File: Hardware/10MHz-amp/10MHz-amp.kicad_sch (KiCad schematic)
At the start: 118 parts, among them J1 Conn_Coaxial, J2 Barrel_Jack_MountingPin, J3 BANANA_JACK, J4 BANANA_JACK, J5 BANANA_JACK, J6 Conn_Coaxial, J7 Conn_01x07_Pin, J8 Conn_01x07_Socket, K1 TQ2-24V, K2 TQ2-24V, K3 TQ2-24V, K4 TQ2-24V, K5 TQ2-24V, K6 TQ2-5V, Q1 PMOS, Q2 PMOS, Q3 NMOS, SW1 SW_SPDT, SW2 SW_SPST, SW3 SW_SP5T_NR01105, U1 THS3491xDDA

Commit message: fixed issues 1-5 and changed relay topo
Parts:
- removed C15: 6.8u, Capacitor_SMD:C_0603_1608Metric, symbol Device:C
- removed D3, D4: PTVS18VZ1USK, Diode_SMD:Nexperia_DSN1608-2_1.6x0.8mm, symbol Diode:PTVS18VZ1USK
- removed D5: PTVS15VZ1USK, Diode_SMD:Nexperia_DSN1608-2_1.6x0.8mm, symbol Diode:PTVS15VZ1USK
- removed D6, D8, D9: D_Zener, Diode_SMD:D_0603_1608Metric, symbol Device:D_Zener
- removed F1: Fuse, symbol Device:Fuse
- removed Q1: PMOS, symbol Simulation_SPICE:PMOS
- removed R8: 10k, Capacitor_SMD:C_0603_1608Metric, symbol Device:R
- added C12: 6.8u, Capacitor_SMD:C_0603_1608Metric, symbol Device:C
- added D13, D26: SMAJ16CA, Diode_SMD:D_SMA, symbol Diode:SMAJ16CA
- added D28, D29, D30: BZV55B10, Diode_SMD:D_MiniMELF, symbol Diode:BZV55B10
- added D3: SMAJ26CA, Diode_SMD:D_SMA, symbol Diode:SMAJ26CA
- added F2: Fuse, symbol Device:Fuse
- added Q4: DMPH6250SQ-13, Package_TO_SOT_SMD:SOT-23-3, symbol Simulation_SPICE:PMOS
- added R33, R6: 1, Capacitor_SMD:C_0603_1608Metric, symbol Device:R
- D12: renamed from D15; value D_Schottky -> NSR0340HT1G
- D17: renamed from D18; Notes 10x -> 6x
- D18: renamed from D19; Notes 50x -> 10x
- D21, D22, D23, D24, D25: value D_Schottky -> NSR0340HT1G
- F1: renamed from F2; Notes (none) -> 700mA
- F3: Notes (none) -> 1A
- Q1: renamed from Q2; value PMOS -> DMPH6250SQ-13; footprint (none) -> Package_TO_SOT_SMD:SOT-23-3; Manufactor Part Number (none) -> DMPH6250SQ-13; Notes (none) -> 60 V 2.4A; Supplier link (none) -> https://www.digikey.co.nz/en/products/detail/diodes-incorpo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
- Q2: renamed from Q3; value NMOS -> DMN6075SQ-7; footprint (none) -> Package_TO_SOT_SMD:SOT-23-3; Manufactor Part Number (none) -> DMN6075SQ-7; Notes (none) -> 60 V 2A; Supplier link (none) -> https://www.digikey.co.nz/en/products/detail/diodes-incorpo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
- R1: renamed from R2; Manufactor Part Number (none) -> PTN16-A01120K1C1; Notes LOG -> REVERSE LOG; Supplier Link (none) -> https://www.digikey.co.nz/en/products/detail/same-sky-forme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; Supplier Part Number (none) -> 2223-PTN16-A01120K1C1-ND; Supplier link (none) -> https://www.digikey.co.nz/en/products/detail/same-sky-forme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
- R10: renamed from R11; value 100 -> 1000R
- R12: renamed from R13; value 50 -> 50R
- R2: renamed from R3; value 20k -> 1k
- R3: renamed from R4; value 10k -> 200
- R4: renamed from R5; value 5k -> 110
- R5: renamed from R6; value 1k -> 10.2
- R7: renamed from R1; value 50 -> 50R
- renumbered C12 to C10, C13 to C11, C17 to C13, C16 to C15, C23 to C16, C7 to C17, C8 to C18, C18 to C19, C19 to C20, C20 to C21, C21 to C22, C22 to C23, C9 to C7, C11 to C8, C10 to C9, D14 to D10, D26 to D11, D16 to D15, D17 to D16, D20 to D19, D10 to D20, D7 to D6, D11 to D7, D12 to D8, D13 to D9, FB2 to FB1, FB3 to FB2, FB1 to FB3, J3 to J2, J4 to J3, J5 to J4, J6 to J5, J2 to J6, JP5 to JP1, JP6 to JP2, JP2 to JP3, JP3 to JP4, JP4 to JP5, JP1 to JP6, K5 to K1, K4 to K2, K2 to K4, K1 to K5, R12 to R11, R15 to R13, R16 to R14, R32 to R15, R23 to R16, R29 to R18, R30 to R19, R31 to R20, R7 to R21, R18 to R22, R19 to R23, R20 to R24, R21 to R25, R22 to R26, R14 to R27, R24 to R28, R25 to R29, R26 to R30, R27 to R31, R28 to R32, R9 to R8, R10 to R9
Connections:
- net +24V: no longer C17.1
- net +VDC: no longer C7.1
- net -VDC: no longer C8.2
- net GND: now also J7.7 (Pin_7), SW3.MP, C12.2, D13.1 (A1), D26.2 (A2), D3.1 (A1); no longer K1.3, K1.8, K2.3, K2.8, K3.3, K3.8, K4.3, K4.8, K5.3, K5.8
- net VCC: now also R11.1; no longer R11.2
- net at R4.2: now also K4.8; no longer K2.4
- net at JP5.2 (B), JP6.1 (A): now also D30.1 (K), Q4.3 (S)
- net at R21.2: now also D30.2 (A), Q4.2 (G)
- net at R5.2: now also K5.8; no longer K1.4
- net at R2.2: now also K2.8; no longer K4.4
- net at J6.1: now also F3.1
- net at JP5.1 (A): now also F3.2, D3.2 (A2), Q4.1 (D)
- net at SW1.1 (A): now also D6.1 (K); no longer R11.1
- net at SW1.2 (B), U1.8 (~{PD}): no longer D6.2 (A)
- net at J7.6 (Pin_6), SW3.5: now also D19.2 (A)
- net at J7.1 (Pin_1), SW3.C (Common): now also C12.1
- net at JP2.1 (A), Q2.1 (D): now also D26.1 (A1), F2.1; no longer F3.2
- net at K5.4: now also K1.4, K2.4, K3.4, K4.4, R10.2, U1.2 (-); no longer R1.2
- net at R3.2: now also K3.8; no longer K3.4
- net at F1.2, JP1.1 (A), Q1.1 (D): now also D13.2 (A2)
- net at JP1.2 (B), JP3.1 (A), Q1.3 (S): now also D29.1 (K)
- net at Q2.2 (G), R9.1: now also D28.1 (K)
- net at JP2.2 (B), JP4.1 (A), Q2.3 (S): now also D28.2 (A)
- net at J4.1 (Pin_1): now also F2.2; no longer F3.1
- net at FB3.1, JP6.2 (B): now also C17.1
- net at FB1.1, JP3.2 (B): now also C7.1
- net at Q1.2 (G), R8.2: now also D29.2 (A)
- net at FB2.1, JP4.2 (B): now also C8.2
- new net: R33.2, R4.1
- new net: K5.3, R5.1
- new net: K2.3, R2.1
- new net: K1.3, R6.1
- new net: R1.1, R6.2
- new net: K1.8, R1.2
- new net: K3.3, R3.1
- new net: K4.3, R33.1
- new net: D6.2 (A), R11.2
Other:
- note added: "24v @ 1A INPUT"
- note added: "50 termination Ohm LOAD"
- note added: "AMP ENABLE"
- note added: "Other common gains with thier resistors"
- note added: "RF"
- note added: "RI"
- note added: "RI = RF/(A_G-1)"
- note removed: "24v @ 2A INPUT"
- note removed: "50 Ohm LOAD"
- moved on the sheet: C1, C10, C11, C13, C14, C15, C16, C17, C18, C19, C2, C20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

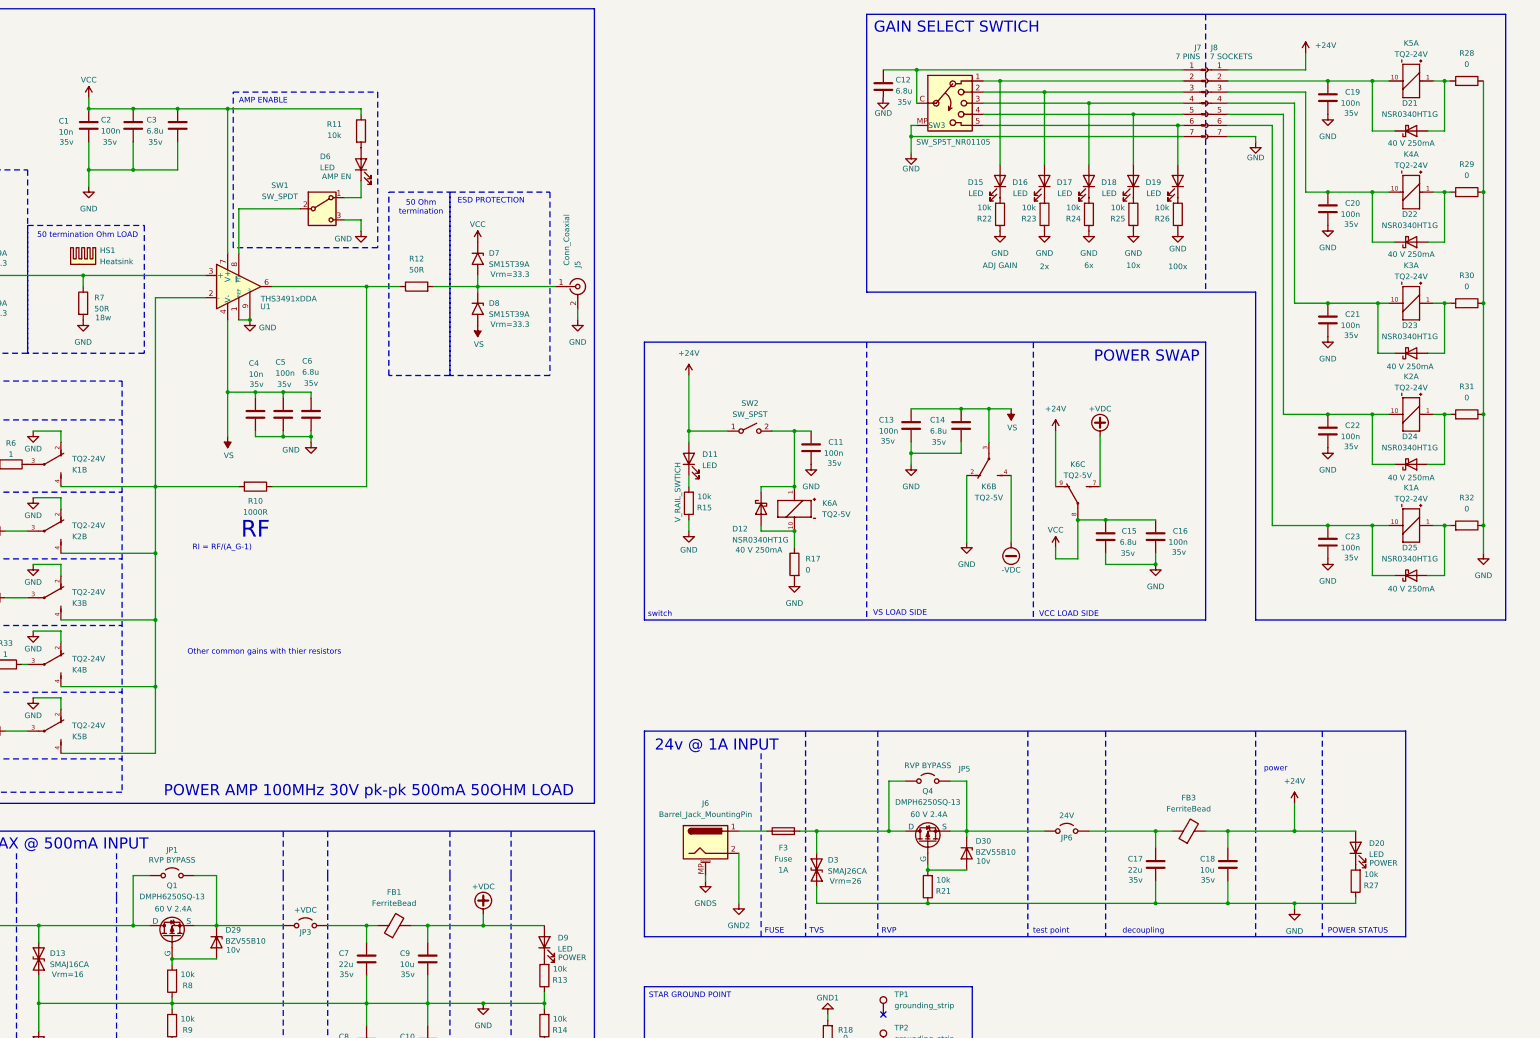
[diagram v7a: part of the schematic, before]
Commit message: added switch to allow for a gain of 1
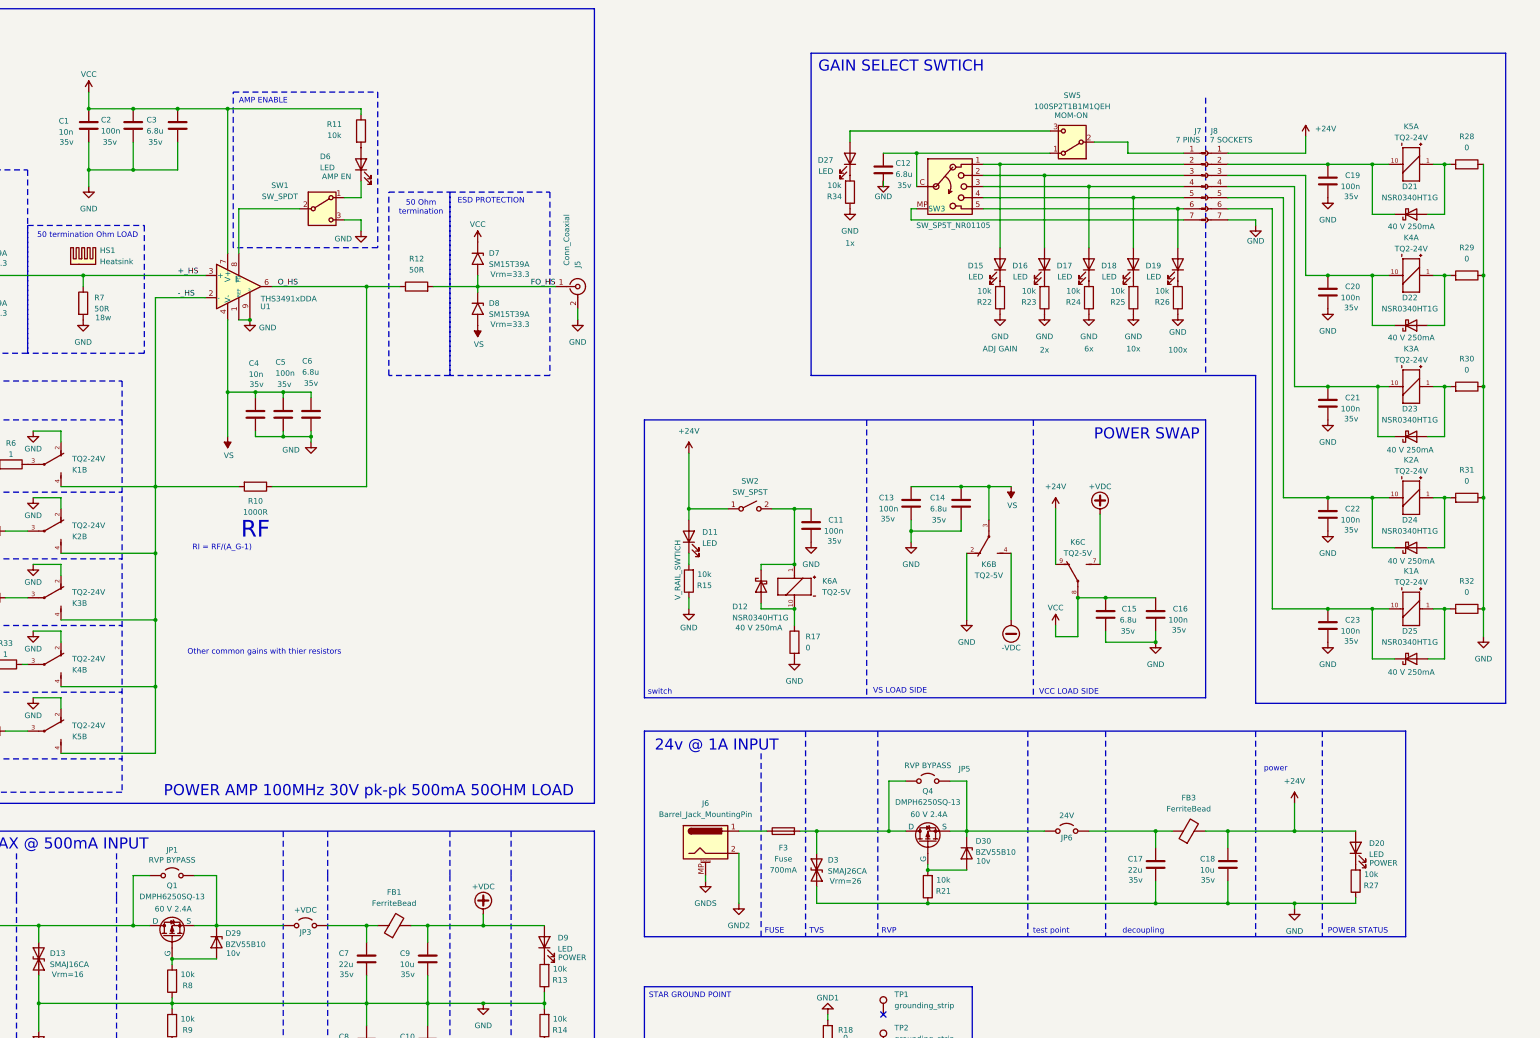
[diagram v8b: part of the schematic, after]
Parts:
- added D27: LED, Diode_SMD:D_0603_1608Metric, symbol Device:LED
- added R34: 10k, Capacitor_SMD:C_0603_1608Metric, symbol Device:R
- added SW5: 100SP2T1B1M1QEH, Connector_PinHeader_2.54mm:PinHeader_1x03_P2.54mm_Vertical, symbol Switch:SW_SPDT
- F3: Notes 1A -> 700mA
- JP3: now left out of the parts list
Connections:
- net GND: now also R34.1; no longer J7.7 (Pin_7), SW3.MP
- net +_HS: now reaches D1.2 (A2), D2.1 (A1), J1.1 (In), R7.1, U1.3 (+)
- net -_HS: now reaches K1.4, K2.4, K3.4, K4.4, K5.4, R10.2, U1.2 (-)
- net at C12.1, SW3.C (Common): now also SW5.1 (A); no longer J7.1 (Pin_1)
- net FO_HS: now reaches D7.2 (A2), D8.1 (A1), J5.1 (In), R12.2
- net O_HS: now reaches R10.1, R12.1, U1.6
- new net: J7.7 (Pin_7), SW3.MP
- new net: D27.1 (K), R34.2
- new net: J7.1 (Pin_1), SW5.2 (B)
- new net: D27.2 (A), SW5.3 (C)
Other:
- moved on the sheet: C11, C12, C13, C14, C15, C16, C19, C20, C21, C22, C23, D11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
